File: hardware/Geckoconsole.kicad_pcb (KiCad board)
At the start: 2 copper layers, 68.6 x 41.9 mm, 53 parts, among them J1 Conn_01x08_Male, J21 I²C, J31 Conn_01x07_Female, J50 USB-C, J71 Conn_01x07, Q51 S8050, Q52 S8050, SW2 Reset, SW41 Rotary_Encoder_Switch, U1 ESP32-WROOM-32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

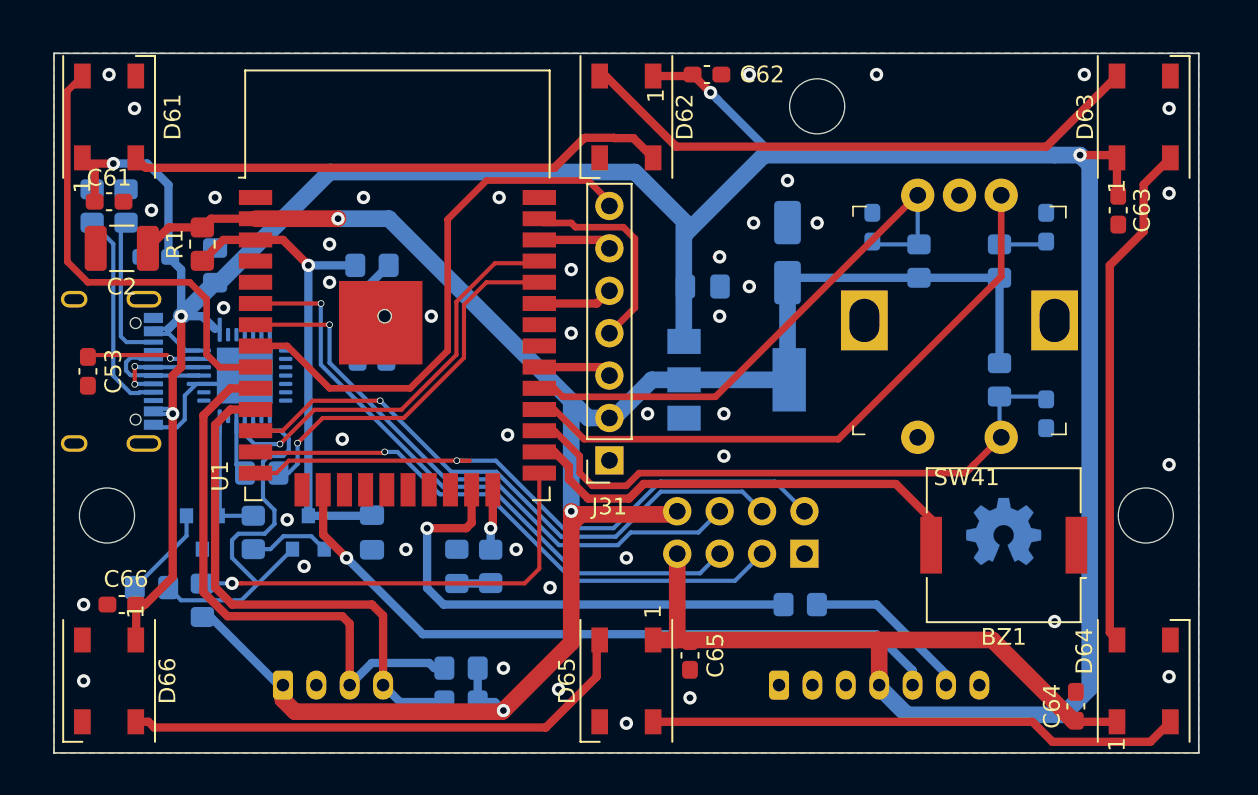
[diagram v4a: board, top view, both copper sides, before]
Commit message: Console PCB: add proximity sensor and level shifting
* Add "break-out" daughterboard for VCNL4040 proximity sensor
* Add diode for WS2812 level shifting
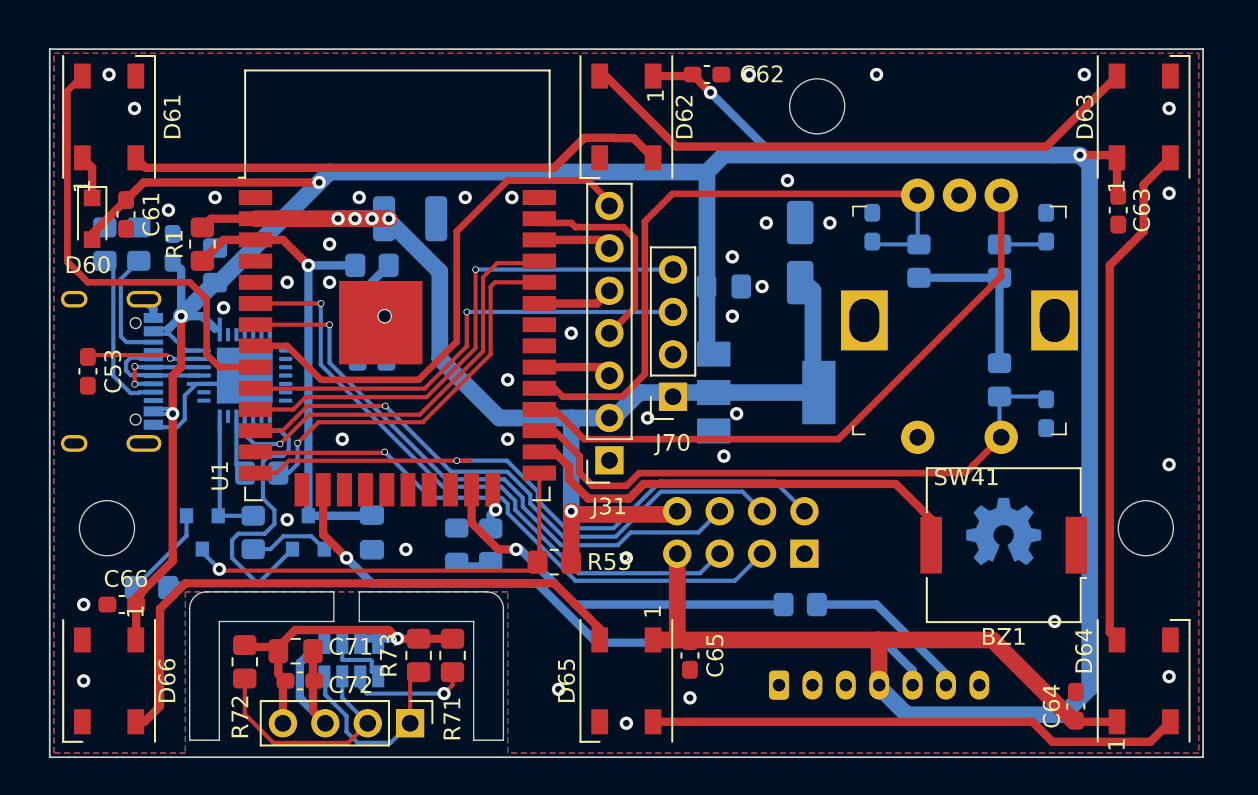
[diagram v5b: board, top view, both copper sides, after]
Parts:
- removed J21: I²C, Connector_JST:JST_PH_B4B-PH-K_1x04_P2.00mm_Vertical
- removed R21, R22: 4k7, Resistor_SMD:R_0805_2012Metric_Pad1.20x1.40mm_HandSolder
- added C71: 100nF, Capacitor_SMD:C_0603_1608Metric_Pad1.08x0.95mm_HandSolder, F.Cu at (65.5, 73.2)
- added C72: 2.2µF, Capacitor_SMD:C_0805_2012Metric_Pad1.18x1.45mm_HandSolder, F.Cu at (65.3, 71.4)
- added D60: 1N4148WS, Diode_SMD:D_SOD-323_HandSoldering, F.Cu at (53.1, 45.5)
- added J70: I²C, Connector_PinSocket_2.54mm:PinSocket_1x04_P2.54mm_Vertical, F.Cu at (87.9, 56.1)
- added J71: I²C, Connector_PinHeader_2.54mm:PinHeader_1x04_P2.54mm_Vertical, F.Cu at (72.1, 75.7)
- added R71: 4k7, Resistor_SMD:R_0805_2012Metric_Pad1.20x1.40mm_HandSolder, F.Cu at (72.6, 71.6)
- added R72: 4k7, Resistor_SMD:R_0805_2012Metric_Pad1.20x1.40mm_HandSolder, F.Cu at (62.2, 72.0)
- added R73: 12k, Resistor_SMD:R_0805_2012Metric_Pad1.20x1.40mm_HandSolder, F.Cu at (74.7, 71.6)
- added U70: VCNL4040M3OE, Fraxinas:VISHAY_VCNL4040_4X2X1.1, B.Cu at (68.6, 71.9)
- C2: moved to B.Cu
- R53: moved to F.Cu
- moved R53 21.2 mm to (80.8, 66.0), turned to 180 degrees
- moved C2 17.4 mm to (72.1, 45.5), turned to 0 degrees
- moved R56 2.41 mm to (53.8, 47.0)
- moved R57 2.41 mm to (55.9, 47.0)
- moved U101 1.93 mm to (93.5, 55.9)
- moved C61 1.27 mm to (55.1, 45.2), turned to 270 degrees
- moved C101 1.27 mm to (90.9, 49.5)
- moved D1 1.27 mm to (74.9, 65.0)
- moved R3 1.27 mm to (77.0, 65.0)
- moved C52 1.14 mm to (57.9, 47.2), turned to 90 degrees
- moved C102 0.76 mm to (95.5, 47.5)
- renumbered J71 to J81, R71 to R81
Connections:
- net /VDD renamed Net-(C53-Pad2)
- D61 pad 1: +5V -> Net-(D60-Pad1)
- R41 pad 2: +3V3 -> Net-(R41-Pad2)
- R42 pad 2: +3V3 -> Net-(R41-Pad2)
- R43 pad 2: +3V3 -> Net-(R41-Pad2)
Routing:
- net +3V3: track 120.6 -> 70.6 mm, vias 3 -> 5
- net VDD: track 0.00 -> 20.7 mm, vias 0 -> 1
- net SDA: track 0.00 -> 14.3 mm
- net SCL: track 0.00 -> 12.0 mm
- net GNDD: track 0.00 -> 11.2 mm
- net Net-(R41-Pad2): track 0.00 -> 9.94 mm
- net Net-(R73-Pad1): track 0.00 -> 7.59 mm, vias 0 -> 1
- net RX1: track 30.2 -> 22.7 mm
- net I2C_SDI: track 34.0 -> 28.1 mm, vias 0 -> 1
- net ENC_B: track 33.7 -> 39.1 mm
- net Net-(D65-Pad2): track 31.3 -> 36.4 mm
- net C-Prox: track 0.00 -> 4.10 mm
- net Net-(D60-Pad1): track 0.00 -> 2.64 mm
- net Net-(J50-PadA5): track 12.5 -> 9.93 mm
- net +5V: track 214.2 -> 216.7 mm
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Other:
- board size 68.6 x 41.9 mm -> 69.1 x 42.4 mm

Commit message: Console Hardware: Convert Geckoconsole to KiCad 6
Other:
- net class Default removed

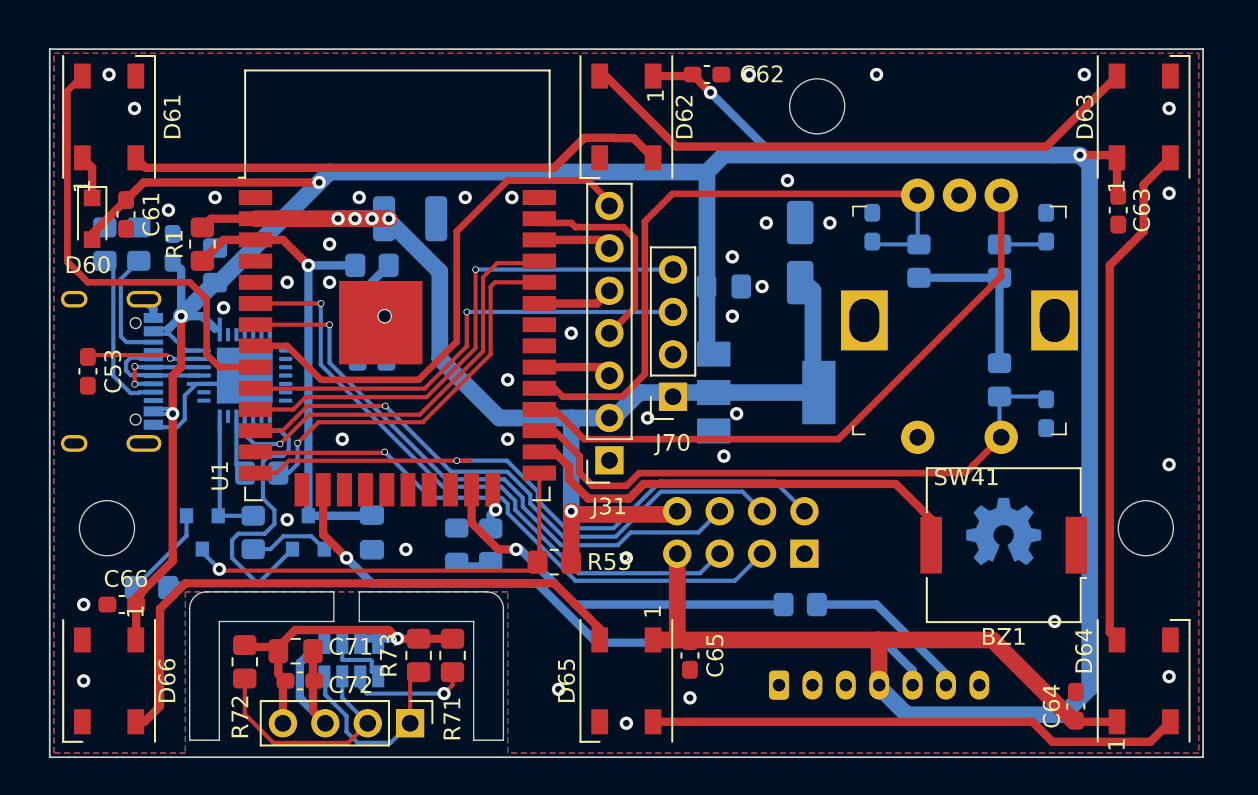
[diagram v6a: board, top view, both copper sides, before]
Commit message: Console Hardware: Fix DRC problems (unconnected traces etc.)
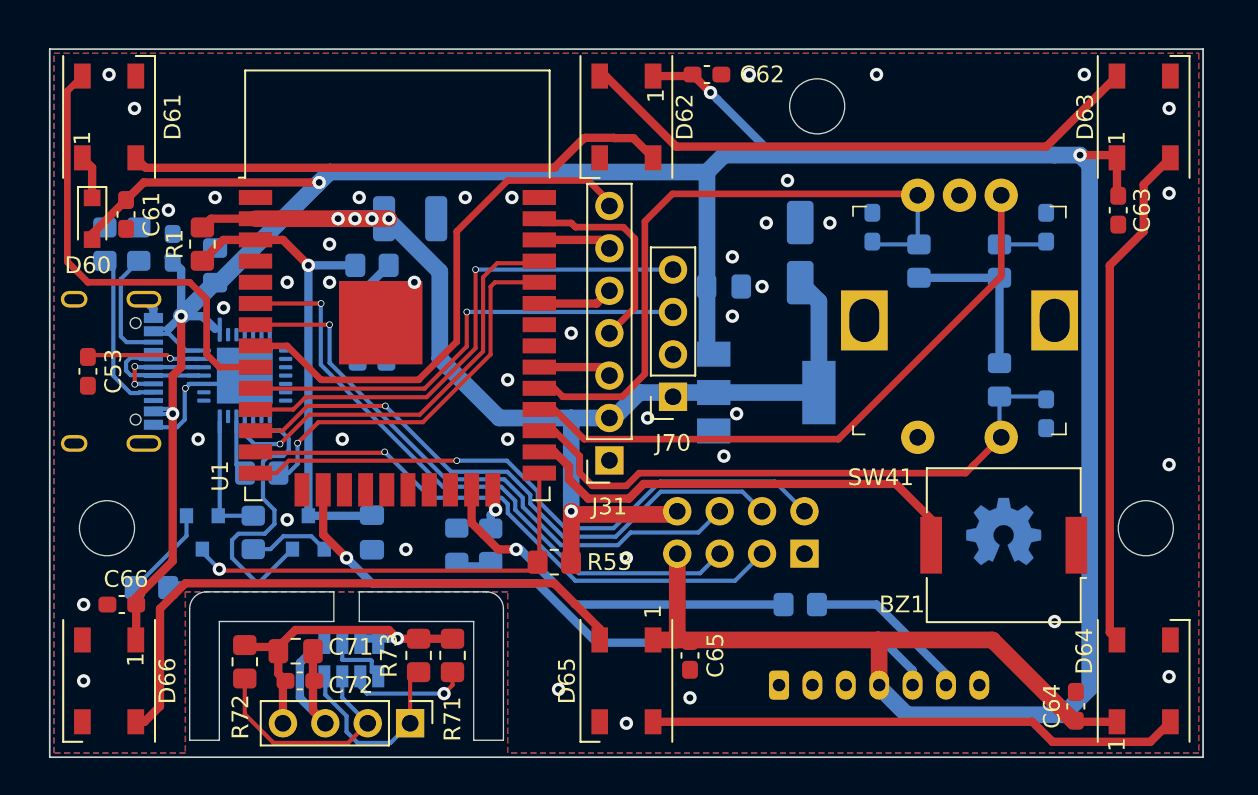
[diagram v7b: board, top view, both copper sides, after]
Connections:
- D66 pad 2: (no net) -> unconnected-(D66-Pad2)
- J50 pad A8: (no net) -> unconnected-(J50-PadA8)
- J50 pad B8: (no net) -> unconnected-(J50-PadB8)
- J81 pad 1: (no net) -> unconnected-(J81-Pad1)
- J81 pad 2: (no net) -> unconnected-(J81-Pad2)
- J81 pad 7: (no net) -> unconnected-(J81-Pad7)
- U1 pad 17: (no net) -> unconnected-(U1-Pad17)
- U1 pad 18: (no net) -> unconnected-(U1-Pad18)
- U1 pad 19: (no net) -> unconnected-(U1-Pad19)
- U1 pad 20: (no net) -> unconnected-(U1-Pad20)
- U1 pad 21: (no net) -> unconnected-(U1-Pad21)
- U1 pad 22: (no net) -> unconnected-(U1-Pad22)
- U1 pad 31: (no net) -> SPI_MISO
- U1 pad 32: (no net) -> unconnected-(U1-Pad32)
- U1 pad 4: (no net) -> unconnected-(U1-Pad4)
- U1 pad 5: (no net) -> unconnected-(U1-Pad5)
- U2 pad 1: (no net) -> unconnected-(U2-Pad1)
- U2 pad 10: (no net) -> unconnected-(U2-Pad10)
- U2 pad 11: (no net) -> unconnected-(U2-Pad11)
- U2 pad 12: (no net) -> unconnected-(U2-Pad12)
- U2 pad 13: (no net) -> unconnected-(U2-Pad13)
- U2 pad 14: (no net) -> unconnected-(U2-Pad14)
- U2 pad 15: (no net) -> unconnected-(U2-Pad15)
- U2 pad 16: (no net) -> unconnected-(U2-Pad16)
- U2 pad 17: (no net) -> unconnected-(U2-Pad17)
- U2 pad 18: (no net) -> unconnected-(U2-Pad18)
- U2 pad 19: (no net) -> unconnected-(U2-Pad19)
- U2 pad 2: (no net) -> unconnected-(U2-Pad2)
- U2 pad 20: (no net) -> unconnected-(U2-Pad20)
- U2 pad 21: (no net) -> unconnected-(U2-Pad21)
- U2 pad 22: (no net) -> unconnected-(U2-Pad22)
- U2 pad 23: (no net) -> unconnected-(U2-Pad23)
- U2 pad 27: (no net) -> unconnected-(U2-Pad27)
- U2 pad 9: (no net) -> unconnected-(U2-Pad9)
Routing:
- net Net-(BZ1-Pad2): track 27.9 -> 26.3 mm
- net +3V3: track 70.6 -> 69.3 mm
- net GPIO12: track 37.8 -> 37.1 mm
- net VDD: track 20.7 -> 20.1 mm
- net GND: track 9.72 -> 9.64 mm, vias 39 -> 43
- net (no net): vias 1 -> 0

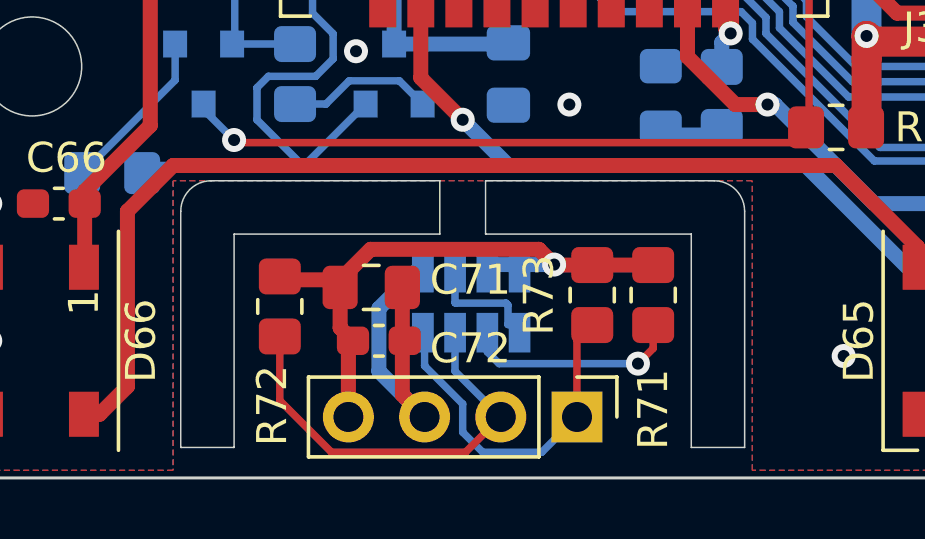
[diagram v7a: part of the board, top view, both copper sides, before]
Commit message: Console PCB: Make ready for fab
* rename layers according to Aisler Gerber specs
* Silkscreen project lable
* break-off-PCB drills
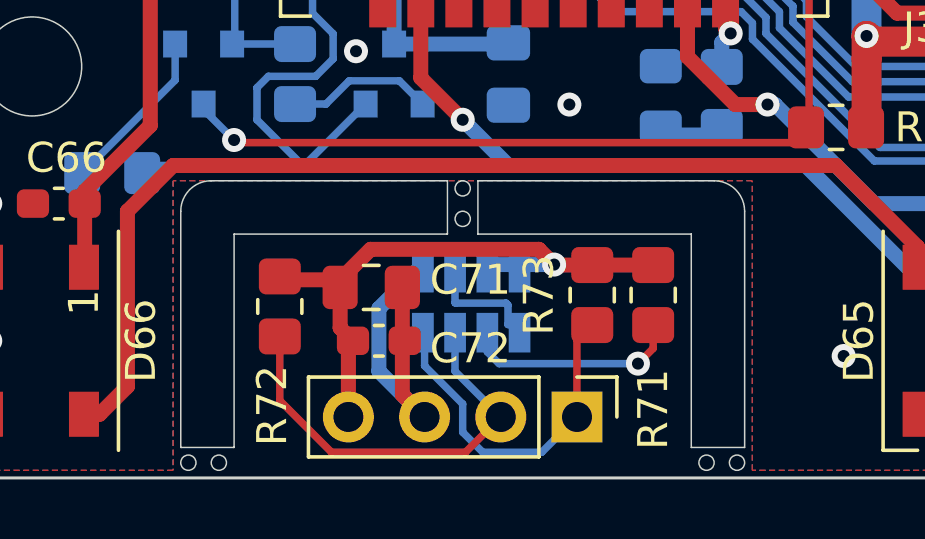
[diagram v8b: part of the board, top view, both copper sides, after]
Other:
- outline, holes or cut-outs redrawn
- board text added: "Gecko Console"
- board text added: "Ver. 1.0 1/2022"
- board text added: "github.com/fraxinas"
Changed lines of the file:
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@@
   (paper "A4")
   (layers
-    (0 "F.Cu" signal)
-    (31 "B.Cu" signal)
+    (0 "F.Cu" signal "toplayer")
+    (31 "B.Cu" signal "bottomlayer")
     (32 "B.Adhes" user "B.Adhesive")
     (33 "F.Adhes" user "F.Adhesive")
-    (34 "B.Paste" user)
-    (35 "F.Paste" user)
-    (36 "B.SilkS" user "B.Silkscreen")
-    (37 "F.SilkS" user "F.Silkscreen")
-    (38 "B.Mask" user)
-    (39 "F.Mask" user)
+    (34 "B.Paste" user "bottompaste")
+    (35 "F.Paste" user "toppaste")
+    (36 "B.SilkS" user "bottomsilkscreen")
+    (37 "F.SilkS" user "topsilkscreen")
+    (38 "B.Mask" user "bottomsoldermask")
+    (39 "F.Mask" user "topsoldermask")
     (40 "Dwgs.User" user "User.Drawings")
     (41 "Cmts.User" user "User.Comments")
     (42 "Eco1.User" user "User.Eco1")
     (43 "Eco2.User" user "User.Eco2")
-    (44 "Edge.Cuts" user)
+    (44 "Edge.Cuts" user "boardoutline")
     (45 "Margin" user)
     (46 "B.CrtYd" user "B.Courtyard")
@@
   )
   (setup
+    (stackup
+      (layer "F.SilkS" (type "Top Silk Screen"))
+      (layer "F.Paste" (type "Top Solder Paste"))
+      (layer "F.Mask" (type "Top Solder Mask") (thickness 0.01))
+      (layer "F.Cu" (type "copper") (thickness 0.035))
+      (layer "dielectric 1" (type "core") (thickness 1.51) (material "FR4") (epsilon_r 4.5) (loss_tangent 0.02))
+      (layer "B.Cu" (type "copper") (thickness 0.035))
+      (layer "B.Mask" (type "Bottom Solder Mask") (thickness 0.01))
+      (layer "B.Paste" (type "Bottom Solder Paste"))
+      (layer "B.SilkS" (type "Bottom Silk Screen"))
+      (copper_finish "None")
+      (dielectric_constraints no)
+    )
     (pad_to_mask_clearance 0)
     (pcbplotparams
@@
   (gr_circle (center 116.206 64.008) (end 117.856 64.008) (layer "Edge.Cuts") (width 0.05) (fill none))
   (gr_circle (center 96.52 38.734) (end 98.17 38.734) (layer "Edge.Cuts") (width 0.05) (fill none))
-  (gr_line (start 67.564 69.596) (end 60.706 69.596) (layer "Edge.Cuts") (width 0.05))
-  (gr_line (start 69.088 67.818) (end 76.708 67.818) (layer "Edge.Cuts") (width 0.05))
-  (gr_line (start 69.088 69.596) (end 75.946 69.596) (layer "Edge.Cuts") (width 0.05))
+  (gr_line (start 67.818 69.596) (end 60.706 69.596) (layer "Edge.Cuts") (width 0.05))
+  (gr_line (start 68.834 67.818) (end 76.708 67.818) (layer "Edge.Cuts") (width 0.05))
+  (gr_line (start 68.834 69.596) (end 75.946 69.596) (layer "Edge.Cuts") (width 0.05))
   (gr_arc (start 58.928 68.834) (mid 59.22558 68.11558) (end 59.944 67.818) (layer "Edge.Cuts") (width 0.05))
   (gr_line (start 75.946 76.708) (end 75.946 69.596) (layer "Edge.Cuts") (width 0.05))
+  (gr_circle (center 68.326 68.072) (end 68.58 68.072) (layer "Edge.Cuts") (width 0.05) (fill none))
   (gr_arc (start 76.708 67.818) (mid 77.42642 68.11558) (end 77.724 68.834) (layer "Edge.Cuts") (width 0.05))
   (gr_line (start 119.634 77.724) (end 50.546 77.724) (layer "Edge.Cuts") (width 0.1))
+  (gr_circle (center 76.454 77.216) (end 76.2 77.216) (layer "Edge.Cuts") (width 0.05) (fill none))
   (gr_line (start 60.706 76.708) (end 58.928 76.708) (layer "Edge.Cuts") (width 0.05))
   (gr_line (start 50.546 77.724) (end 50.546 35.306) (layer "Edge.Cuts") (width 0.1))
   (gr_line (start 77.724 76.708) (end 77.724 68.834) (layer "Edge.Cuts") (width 0.05))
-  (gr_line (start 69.088 69.596) (end 69.088 67.818) (layer "Edge.Cuts") (width 0.05))
+  (gr_line (start 68.834 69.596) (end 68.834 67.818) (layer "Edge.Cuts") (width 0.05))
+  (gr_circle (center 60.198 77.216) (end 60.452 77.216) (layer "Edge.Cuts") (width 0.05) (fill none))
   (gr_circle (center 53.976 64.008) (end 55.626 64.008) (layer "Edge.Cuts") (width 0.05) (fill none))
-  (gr_line (start 67.564 69.596) (end 67.564 67.818) (layer "Edge.Cuts") (width 0.05))
+  (gr_line (start 67.818 69.596) (end 67.818 67.818) (layer "Edge.Cuts") (width 0.05))
   (gr_line (start 75.946 76.708) (end 77.724 76.708) (layer "Edge.Cuts") (width 0.05))
   (gr_line (start 58.928 76.708) (end 58.928 68.834) (layer "Edge.Cuts") (width 0.05))
-  (gr_line (start 67.564 67.818) (end 59.944 67.818) (layer "Edge.Cuts") (width 0.05))
+  (gr_line (start 67.818 67.818) (end 59.944 67.818) (layer "Edge.Cuts") (width 0.05))
+  (gr_circle (center 77.47 77.216) (end 77.216 77.216) (layer "Edge.Cuts") (width 0.05) (fill none))
   (gr_line (start 119.634 35.306) (end 119.634 77.724) (layer "Edge.Cuts") (width 0.1))
   (gr_line (start 50.546 35.306) (end 119.634 35.306) (layer "Edge.Cuts") (width 0.1))
+  (gr_circle (center 59.182 77.216) (end 59.436 77.216) (layer "Edge.Cuts") (width 0.05) (fill none))
+  (gr_circle (center 68.326 69.088) (end 68.58 69.088) (layer "Edge.Cuts") (width 0.05) (fill none))
   (gr_line (start 60.706 69.596) (end 60.706 76.708) (layer "Edge.Cuts") (width 0.05))
+  (gr_text "Gecko Console" (at 71.12 37.084) (layer "B.SilkS")
+    (effects (font (size 1.5 1.5) (thickness 0.15)) (justify mirror))
+  )
+  (gr_text "github.com/fraxinas" (at 71.374 40.386) (layer "B.SilkS")
+    (effects (font (size 1.25 1.25) (thickness 0.15)) (justify mirror))
+  )
+  (gr_text "Ver. 1.0 1/2022" (at 70.866 38.862) (layer "B.SilkS")
+    (effects (font (size 1 1) (thickness 0.15)) (justify mirror))
+  )
   (gr_text "Reset" (at 75.184 52.07) (layer "B.SilkS")
     (effects (font (size 1 1) (thickness 0.2)) (justify mirror))
